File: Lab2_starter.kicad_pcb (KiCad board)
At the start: 4 copper layers, 123.2 x 64.6 mm, 78 parts, among them J1 973582101, J10 Conn_01x02, J11 Conn_01x02, J12 Conn_01x02, J13 Conn_01x02, J14 Conn_01x02, J15 Conn_01x02, J16 Conn_01x02, J2 973582100, J3 973582101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

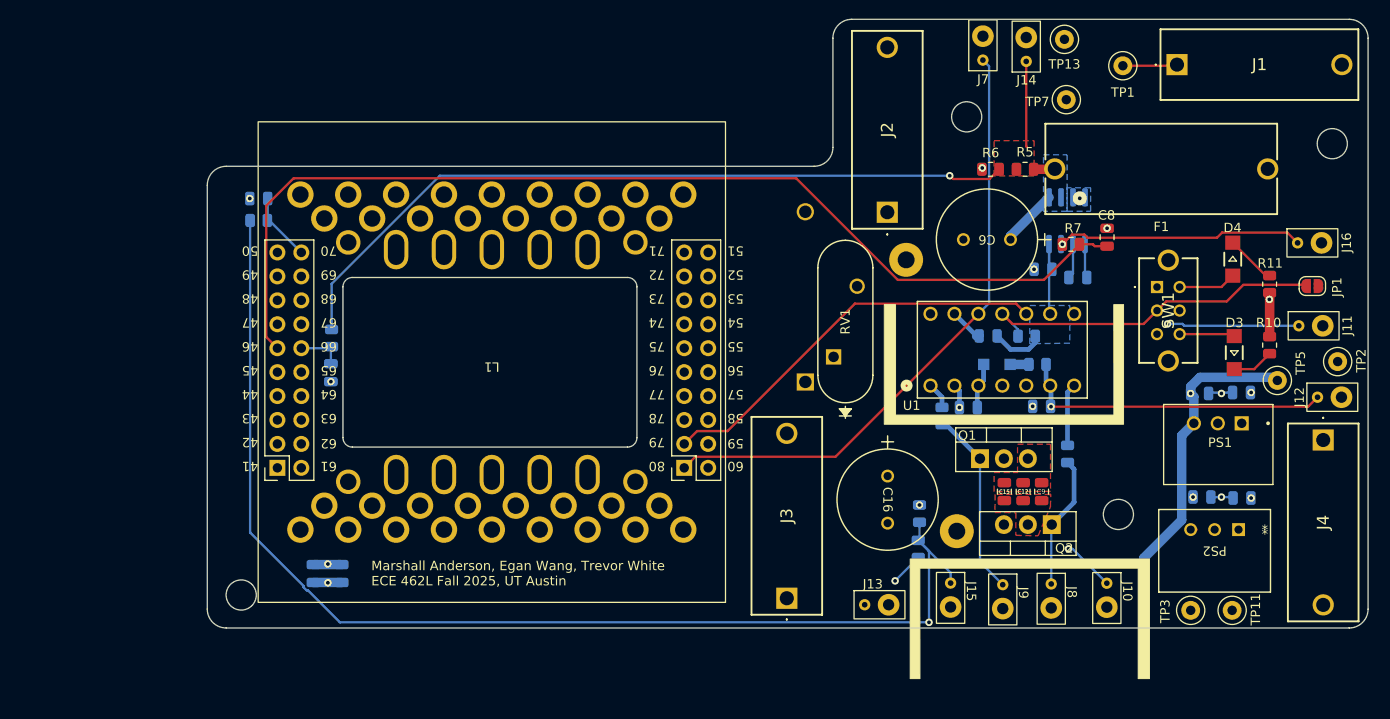
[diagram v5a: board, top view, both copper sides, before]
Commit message: further reduced board size, reworked V_sw node as trace instead of pour, moved V_out pour to front layer and thickened
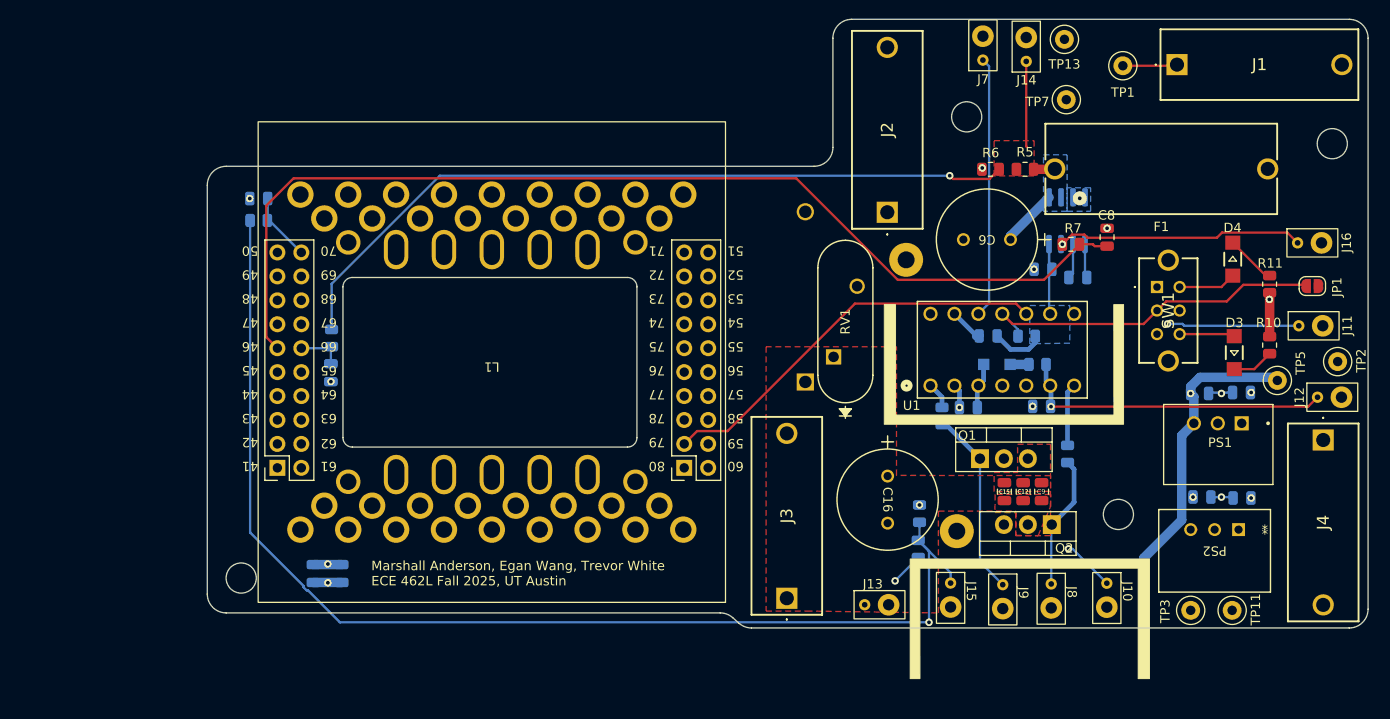
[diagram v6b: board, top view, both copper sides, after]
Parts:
- moved H1 1.80 mm to (34.6, 92.7)
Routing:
- net Vsw: track 5.84 -> 44.9 mm
- removed copper zone on In1.Cu, net Vout
- removed copper zone on In2.Cu, net Vsw
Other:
- outline, holes or cut-outs redrawn
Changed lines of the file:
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@@
 	(footprint "MountingHole:MountingHole_3.2mm_M3"
 		(layer "F.Cu")
-		(at 34.6 94.5)
+		(at 34.6 92.7)
 		(descr "Mounting Hole 3.2mm, no annular, M3")
 		(tags "mounting hole 3.2mm no annular m3")
@@
 		(layer "B.SilkS")
 	)
+	(gr_arc
+		(start 33 96.4)
+		(mid 31.585786 95.814214)
+		(end 31 94.4)
+		(stroke
+			(width 0.1)
+			(type default)
+		)
+		(layer "Edge.Cuts")
+	)
 	(gr_line
 		(start 46.4 60.8)
@@
 	)
 	(gr_line
+		(start 33 96.4)
+		(end 85.439601 96.4)
+		(stroke
+			(width 0.1)
+			(type default)
+		)
+		(layer "Edge.Cuts")
+	)
+	(gr_line
 		(start 97.4 47)
 		(end 97.4 35.4)
@@
 	(gr_line
 		(start 152.2 98)
-		(end 33 98)
+		(end 88.760399 98)
 		(stroke
 			(width 0.1)
@@
 	)
 	(gr_arc
-		(start 33 98)
-		(mid 31.585786 97.414214)
-		(end 31 96)
-		(stroke
-			(width 0.1)
-			(type default)
-		)
-		(layer "Edge.Cuts")
-	)
-	(gr_arc
 		(start 75.6 60.8)
 		(mid 76.307107 61.092893)
@@
 	)
 	(gr_arc
+		(start 88.760399 98)
+		(mid 88.049638 97.869443)
+		(end 87.431671 97.494819)
+		(stroke
+			(width 0.1)
+			(type default)
+		)
+		(layer "Edge.Cuts")
+	)
+	(gr_arc
 		(start 45.4 61.8)
 		(mid 45.692893 61.092893)
@@
 	)
 	(gr_line
-		(start 31 96)
+		(start 31 94.4)
 		(end 31 51)
 		(stroke
@@
 		(layer "Edge.Cuts")
 	)
+	(gr_arc
+		(start 85.439601 96.4)
+		(mid 86.150362 96.530557)
+		(end 86.768329 96.905181)
+		(stroke
+			(width 0.1)
+			(type default)
+		)
+		(layer "Edge.Cuts")
+	)
 	(gr_line
 		(start 75.6 78.8)
@@
 	)
 	(gr_line
+		(start 86.768329 96.905181)
+		(end 87.431671 97.494819)
+		(stroke
+			(width 0.1)
+			(type default)
+		)
+		(layer "Edge.Cuts")
+	)
+	(gr_line
 		(start 99.4 33.4)
 		(end 152.2 33.4)
@@
 		(net 16)
 	)
+	(segment
+		(start 122.8 88.711922)
+		(end 122.8 78.677422)
+		(width 1.5)
+		(layer "In2.Cu")
+		(net 16)
+	)
+	(segment
+		(start 122.8 78.677422)
+		(end 118.6 74.477422)
+		(width 1.5)
+		(layer "In2.Cu")
+		(net 16)
+	)
+	(segment
+		(start 122.5335 88.978422)
+		(end 122.8 88.711922)
+		(width 1.5)
+		(layer "In2.Cu")
+		(net 16)
+	)
+	(segment
+		(start 115.55 80.027422)
+		(end 115.55 87.027422)
+		(width 1.5)
+		(layer "In2.Cu")
+		(net 16)
+	)
+	(segment
+		(start 115.55 87.226878)
+		(end 117.301544 88.978422)
+		(width 1.5)
+		(layer "In2.Cu")
+		(net 16)
+	)
+	(segment
+		(start 115.55 87.027422)
+		(end 115.55 87.226878)
+		(width 1.5)
+		(layer "In2.Cu")
+		(net 16)
+	)
+	(segment
+		(start 117.301544 88.978422)
+		(end 122.5335 88.978422)
+		(width 1.5)
+		(layer "In2.Cu")
+		(net 16)
+	)
+	(segment
+		(start 110.55 87.727422)
+		(end 114.85 87.727422)
+		(width 1.5)
+		(layer "In2.Cu")
+		(net 16)
+	)
+	(segment
+		(start 118.6 74.477422)
+		(end 118.6 72.957422)
+		(width 1.5)
+		(layer "In2.Cu")
+		(net 16)
+	)
+	(segment
+		(start 118.6 72.957422)
+		(end 117.92 72.277422)
+		(width 1.5)
+		(layer "In2.Cu")
+		(net 16)
+	)
+	(segment
+		(start 114.85 87.727422)
+		(end 115.55 87.027422)
+		(width 1.5)
+		(layer "In2.Cu")
+		(net 16)
+	)
 	(via
 		(at 123.6 52.4)
@@
 	)
 	(segment
-		(start 82.796 79.829)
-		(end 97.668422 79.829)
+		(start 113.319882 37.727422)
+		(end 113.976 38.38354)
 		(width 0.25)
-		(layer "F.Cu")
+		(layer "B.Cu")
 		(net 18)
 	)
 	(segment
-		(start 81.62 81.005)
-		(end 82.796 79.829)
+		(start 113.976 38.38354)
+		(end 113.976 63.521422)
 		(width 0.25)
-		(layer "F.Cu")
+		(layer "B.Cu")
 		(net 18)
 	)
 	(segment
-		(start 97.668422 79.829)
+		(start 113.976 63.521422)
 		(end 112.84 64.657422)
 		(width 0.25)
-		(layer "F.Cu")
+		(layer "B.Cu")
 		(net 18)
 	)
 	(segment
-		(start 113.319882 37.727422)
-		(end 113.976 38.38354)
+		(start 82.796 79.829)
+		(end 97.668422 79.829)
 		(width 0.25)
-		(layer "B.Cu")
+		(layer "In2.Cu")
 		(net 18)
 	)
 	(segment
-		(start 113.976 38.38354)
-		(end 113.976 63.521422)
+		(start 81.62 81.005)
+		(end 82.796 79.829)
 		(width 0.25)
-		(layer "B.Cu")
+		(layer "In2.Cu")
 		(net 18)
 	)
 	(segment
-		(start 113.976 63.521422)
+		(start 97.668422 79.829)
 		(end 112.84 64.657422)
 		(width 0.25)
-		(layer "B.Cu")
+		(layer "In2.Cu")
 		(net 18)
 	)
@@
 		(layer "F.Cu")
 		(hatch edge 0.5)
+		(priority 9)
+		(connect_pads yes
+			(clearance 0.5)
+		)
+		(min_thickness 0.25)
+		(filled_areas_thickness no)
+		(fill yes
+			(thermal_gap 0.5)
+			(thermal_bridge_width 0.5)
+		)
+		(polygon
+			(pts
+				(xy 90.3 96.2) (xy 94.6 96.2) (xy 108.6 96.4) (xy 108.6 85.6) (xy 116.8 85.6) (xy 116.8 88.2) (xy 120.5 88.2)
+				(xy 120.5 81.82581) (xy 104.15 81.807051) (xy 104.15 68.15) (xy 90.3 68.15)
+			)
+		)
+	)
+	(zone
+		(net 11)
+		(net_name "Vout")
+		(layer "F.Cu")
+		(hatch edge 0.5)
 		(priority 8)
 		(connect_pads yes
@@
 		(polygon
 			(pts
-				(xy 108.6 85.8) (xy 108.6 90.2) (xy 123.8 90.2) (xy 123.8 81.4) (xy 120.6 81.4) (xy 120.6 85.6)
-				(xy 119 85.6) (xy 119.1 88.2) (xy 116.8 88.2) (xy 116.8 85.8)
-			)
-		)
-	)
-	(zone
-		(net 11)
-		(net_name "Vout")
-		(layer "In1.Cu")
-		(hatch edge 0.5)
-		(priority 9)
-		(connect_pads yes
-			(clearance 0.5)
-		)
-		(min_thickness 0.25)
-		(filled_areas_thickness no)
-		(fill yes
-			(thermal_gap 0.5)
-			(thermal_bridge_width 0.5)
-		)
-		(polygon
-			(pts
-				(xy 90.3 96.2) (xy 94.6 96.2) (xy 94.6 85.6) (xy 116.8 85.6) (xy 116.8 88.2) (xy 119.1 88.2) (xy 119.1 83.821685)
-				(xy 104.15 83.804532) (xy 104.15 68.15) (xy 90.3 68.15)
+				(xy 108.6 85.8) (xy 108.6 89.8) (xy 123.6 89.8) (xy 123.6 81.4) (xy 122 81.4) (xy 122 85.6) (xy 119 85.6)
+				(xy 119.1 88.2) (xy 116.8 88.2) (xy 116.8 85.8)
 			)
 		)
@@
 			)
 		)
-	)
-	(zone
-		(net 16)
-		(net_name "Vsw")
-		(layer "In2.Cu")
-		(hatch edge 0.5)
-		(priority 3)
-		(connect_pads yes
-			(clearance 0.5)
-		)
-		(min_thickness 0.25)
-		(filled_areas_thickness no)
-		(fill yes
-			(thermal_gap 0.5)
-			(thermal_bridge_width 0.5)
-		)
-		(polygon
-			(pts
-				(xy 116.8 78.6) (xy 114.4 78.6) (xy 114.4 85.8) (xy 108.6 85.8) (xy 108.6 90.2) (xy 123.8 90.2)
-				(xy 123.8 71.2) (xy 116.8 71.2) (xy 116.8 74.057143) (xy 120.6 78.4) (xy 120.6 88.2) (xy 116.8 88.2)
-			)
-		)

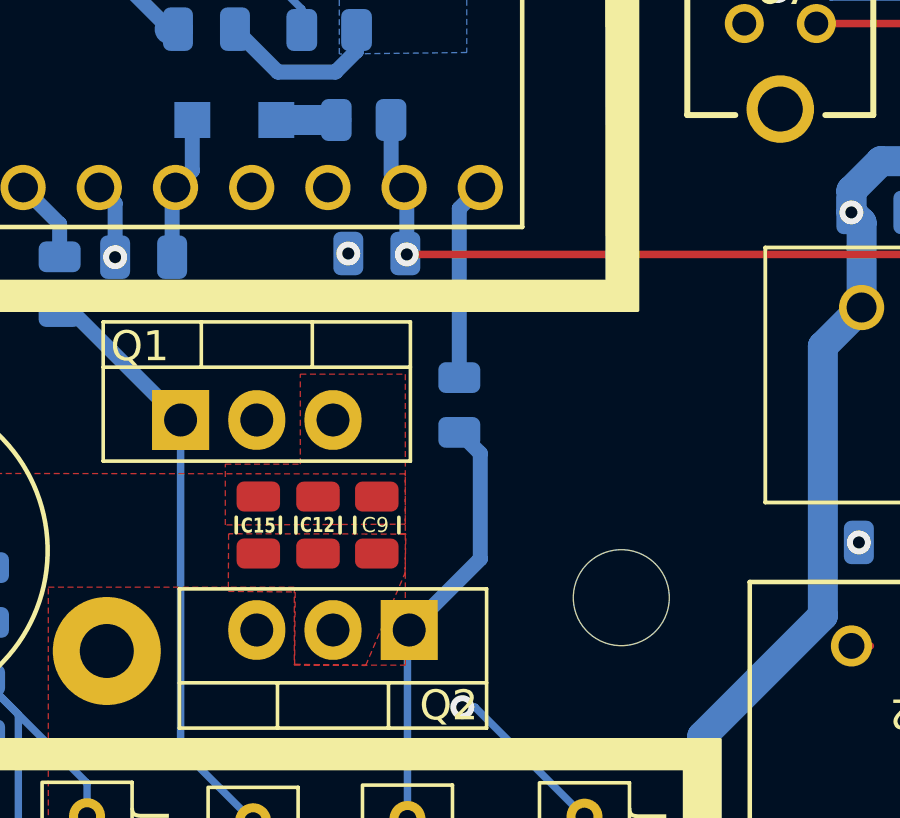
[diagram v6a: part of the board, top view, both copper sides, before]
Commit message: added elon inflation
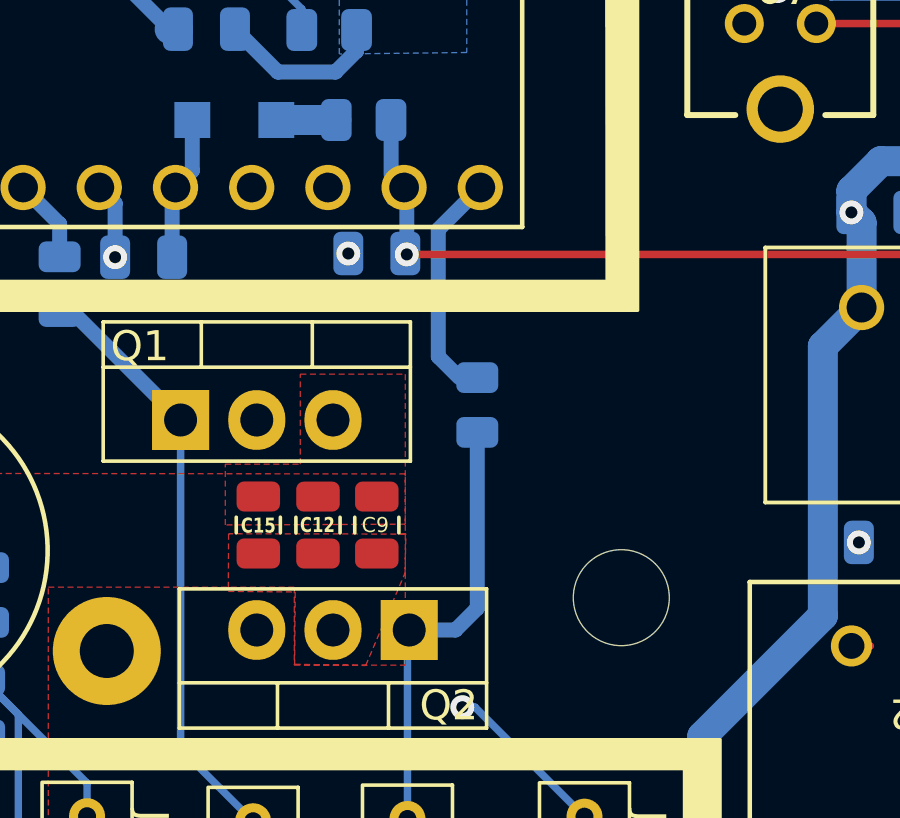
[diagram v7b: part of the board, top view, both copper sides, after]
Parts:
- added G***: LOGO, funnygraphics:elonflation, B.Cu at (149.2, 84.0)
- moved R4 0.60 mm to (122.9, 79.5)
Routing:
- net Vsw: track 44.9 -> 39.6 mm
- net Net-(U1-HO): track 6.63 -> 7.21 mm
- net D': track 14.2 -> 14.8 mm
- added copper zone on In2.Cu, net Vsw
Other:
- board text added: "↑RECESSION ↑INDICATOR"
